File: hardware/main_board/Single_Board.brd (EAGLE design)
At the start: 49.9 x 49.5 mm, 46 parts, among them J1 5520425-3, J2 U.FL, J3 AVR_SPI_PROG_3X2NS, Q1 200mA/40V, Q2 220mA/50V/3.5Ω, Q3 500mA/300V, U1 INA199A3DCKR, U2 MCP1703T-3302E/CB, U3 W25X40CLSNIG, U5 ATMEGA328PB-AU, X1 32.768KHZ-FC-135, X2 B2B-PH-K-S, X3 B2B-XH-2

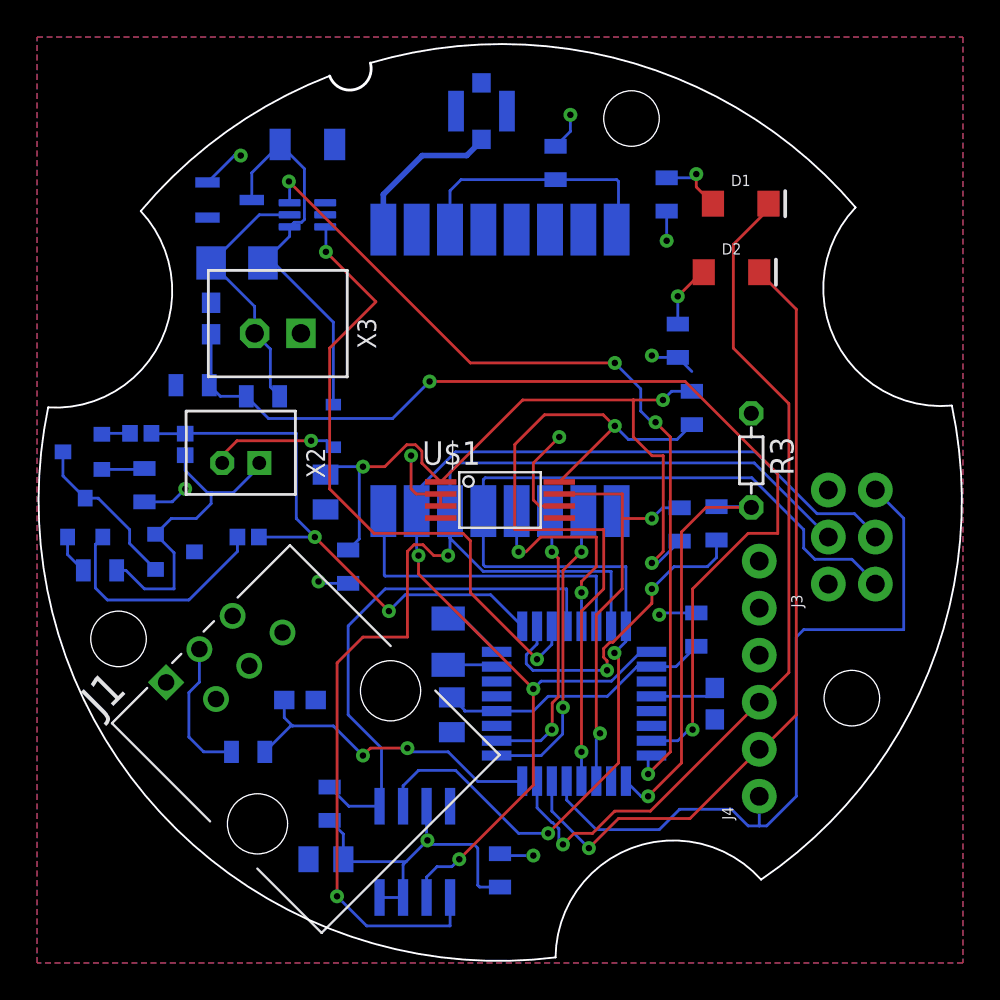
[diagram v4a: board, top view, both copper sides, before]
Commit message: Station improvements. Multi-subpacket handling in receiver. Out of order packets in site datamanager.
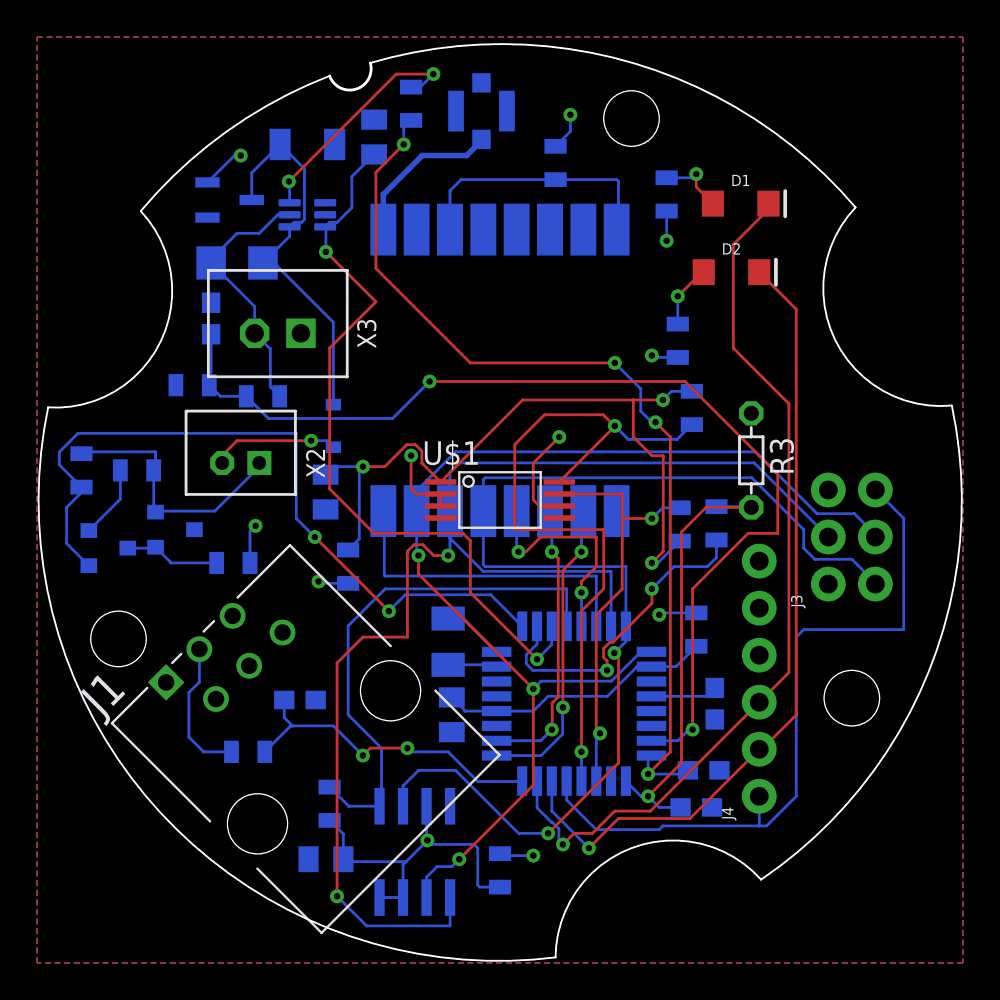
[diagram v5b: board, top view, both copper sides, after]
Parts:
- removed Q3: 500mA/300V, SparkFun-DiscreteSemi:SOT23-3
- removed R19, R20: 500k, SparkFun-Resistors:0402
- added C4, C8: 10nF, SparkFun-Capacitors:0603
- added C9: 1uF, capsmd:0805
- added R15: 10k, SparkFun-Resistors:0805
- Q1: value 200mA/40V -> 220mA/50V/3.5Ω
- R13: value 0 -> 200
- R14: value 20k -> 6k; device SparkFun-Resistors:0402 -> SparkFun-Resistors:0805
- R18: value 0 -> 42k
- R7, R8: value 68k -> 220k
- moved R18 25.1 mm to (20.2, 46.4), turned to 90 degrees
- moved R14 5.77 mm to (2.40, 26.6)
- moved R13 5.76 mm to (5.40, 26.6)
- moved Q1 5.36 mm to (3.80, 22.4), turned to 90 degrees
- moved Q2 1.20 mm to (7.40, 23.4)
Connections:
- removed net N$12: Q1.3, Q2.1, Q3.3
- removed net N$13: Q1.1, R19.1
- net CUR_SENSE: now also C8.2, R18.1; no longer U1.6
- net CUR_SENSE_PWR: now also C9.2
- net GND: now also C4.1, C8.1, C9.1
- net N$10: now also Q1.3, Q2.1, R15.1; no longer Q3.1, R20.1
- net N$3: now also R13.1; no longer R18.1
- net N$5: now also R18.2, U1.6; no longer Q3.2, R13.1
- net N$9: now also R14.2; no longer R14.1
- net PWM_SOLAR: now also Q1.1, R14.1; no longer R14.2, R19.2, R20.2
- net TEMP_SENSE: now also C4.2
- net VCC: now also R15.2; no longer R18.2
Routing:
- net N$5: track 2.15 -> 13.3 mm, vias 0 -> 2
- net PWM_SOLAR: track 30.8 -> 40.6 mm
- net N$12: track 8.83 -> 0.00 mm
- net N$10: track 12.7 -> 5.20 mm
- net CUR_SENSE_PWR: track 35.1 -> 40.3 mm
- net CUR_SENSE: track 48.0 -> 51.2 mm
- net N$9: track 17.3 -> 14.2 mm
- net TEMP_SENSE: track 22.8 -> 24.8 mm
- net N$3: track 2.32 -> 3.95 mm
- net N$13: track 1.54 -> 0.00 mm
- net VCC: track 17.0 -> 15.5 mm
- net AT_RST: track 39.9 -> 39.2 mm

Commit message: Added config for new board Updated Solar PWM for current sensor and impedance switching Fixed a bug with internal termperature sense Added more charge info to detailed weather messages Added support for AVRISP programmer Finalized new board
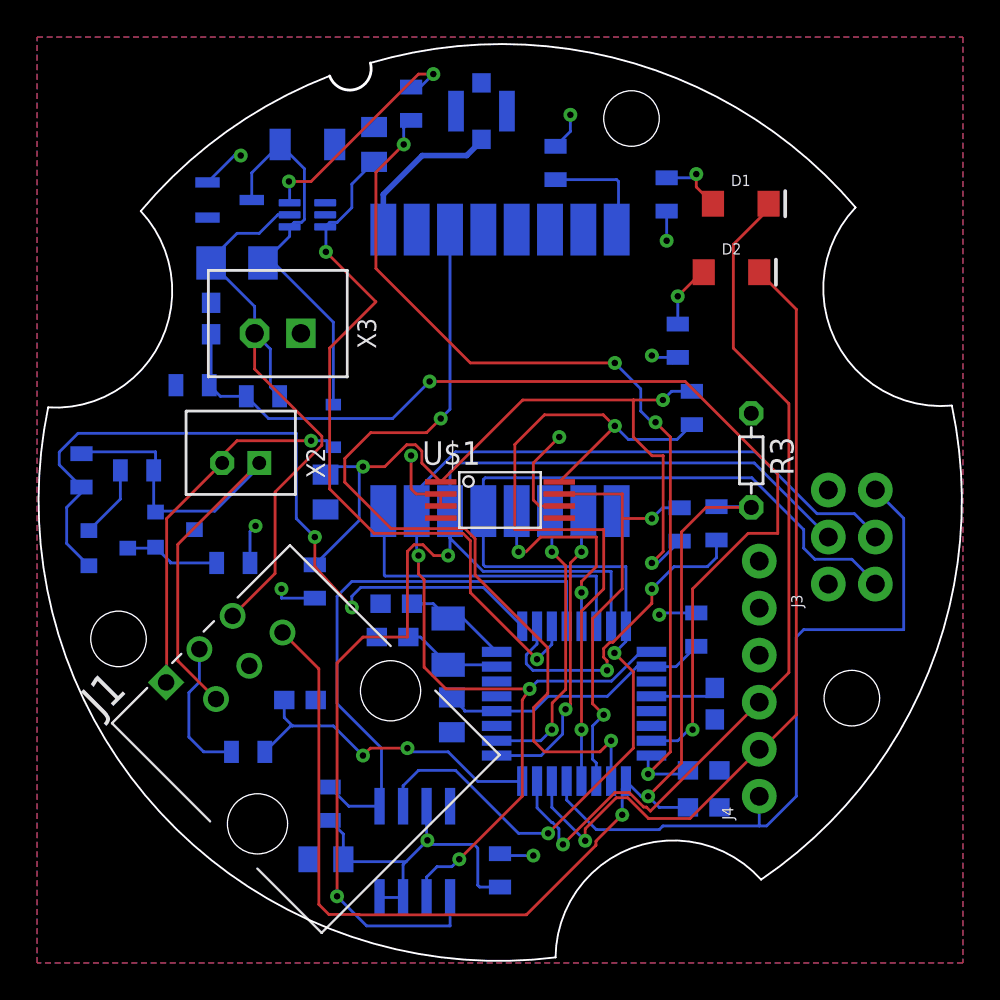
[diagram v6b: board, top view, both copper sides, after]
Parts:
- added C10: 6pF, SparkFun-Capacitors:0603
- added C12: 12pF, SparkFun-Capacitors:0603
- D3: value 0.5A/40V/420mV -> NSR0240HT1G
- Q1: value 220mA/50V/3.5Ω -> 2N7002
- Q2: value 220mA/50V/3.5Ω -> AO3400A
- R13: value 200 -> 20
- R14: value 6k -> 5.6k
- R15: value 10k -> 3.3k
- R18: value 42k -> 47k
- moved R17 1.97 mm to (15.0, 20.6)
- moved C4 0.40 mm to (36.0, 8.40)
- moved C9 0.40 mm to (18.2, 44.2)
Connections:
- removed net N$11: R21.1, R7.1, U1.5, X3.2
- removed net N$9: Q2.2, R13.2, R14.2, X2.1
- new net BATT_+VE: J1.5, R21.1, R7.1, U1.5, X3.2
- new net SOLAR_NEG: J1.2, Q2.2, R13.2, R14.2, X2.1
- new net SX_SW: U$2.SW, U5.26
- net GND: now also C10.1, C12.1
- net N$1: no longer U$2.SW
- net N$7: now also C10.2
- net N$8: now also C12.2
- net TEMP_SENSE: now also J1.6
- net VSOLAR: now also J1.1
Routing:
- net SX_SW: track 0.00 -> 45.8 mm, vias 0 -> 2
- net TEMP_SENSE: track 24.8 -> 61.5 mm, vias 1 -> 2
- net BATT_+VE: track 0.00 -> 32.9 mm
- net SOLAR_NEG: track 0.00 -> 29.6 mm
- net N$11: track 14.2 -> 0.00 mm
- net N$9: track 14.2 -> 0.00 mm
- net VSOLAR: track 6.88 -> 20.0 mm
- net N$1: track 14.1 -> 6.08 mm
- net N$7: track 2.66 -> 5.43 mm
- net SCK: track 62.3 -> 64.9 mm
- net FLASH_SS: track 28.3 -> 30.7 mm
- net N$8: track 3.37 -> 5.65 mm
- net MAG_VCC: track 40.5 -> 42.0 mm
- net PWM_SOLAR: track 40.6 -> 42.1 mm
- net RX: track 43.5 -> 44.3 mm
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
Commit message: Board improvements: Current sensor less prone to latchup Reset pull up resistor JST SH battery connector 8p8c connector to remove shared grounds NPN transistor so we don't operate the mcu outside of spec
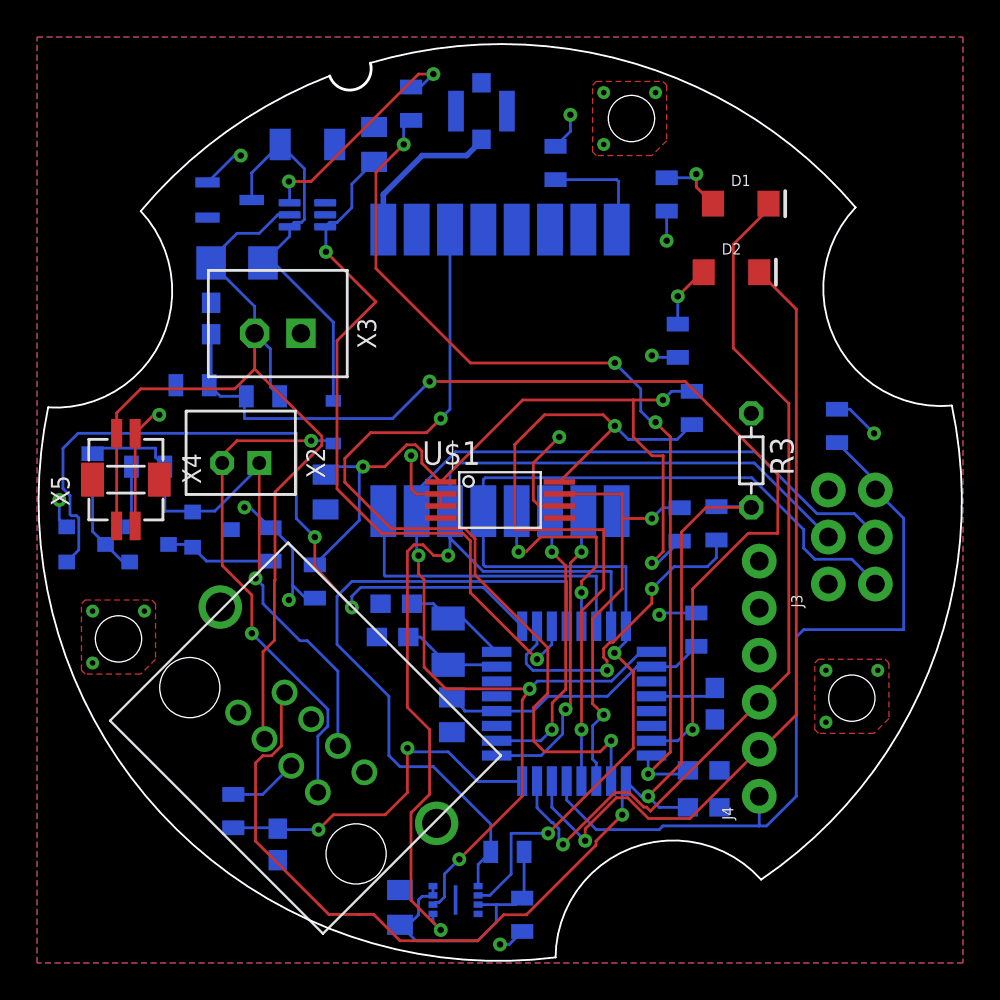
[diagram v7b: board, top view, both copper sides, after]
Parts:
- removed J1: 5520425-3, main_board:TE_5520425-3
- removed U3: W25X40CLSNIG, my-components:WIN_SN-8
- added Q3: S9015, SparkFun-DiscreteSemi:SOT23-3
- added R19: 10k, SparkFun-Resistors:0805
- added U$3: (no value), main_board:RJHSE-3380
- added U4: W25X40CLUXIG_TR, main_board:PSON50P300X200X60-9N
- added X4, X5: BM02B-SRSS-TB, main_board:BM02B-SRSS-TB
- U1: value INA199A3DCKR -> INA199B3DCKR
- U2: value MCP1703T-3302E/CB -> ME6206A25M3G
- moved R9 9.95 mm to (25.4, 6.00), turned to 0 degrees
- moved C2 7.89 mm to (13.0, 6.40), turned to 90 degrees
- moved C7 4.77 mm to (19.6, 3.00), turned to 270 degrees
- moved R6 3.30 mm to (10.6, 8.20), turned to 270 degrees
- moved R16 2.68 mm to (26.2, 2.60), turned to 270 degrees
- moved R15 2.24 mm to (12.6, 22.6), turned to 90 degrees
- moved Q1 2.21 mm to (6.00, 22.6)
- moved Q2 2.00 mm to (9.40, 23.4)
- moved R13 0.63 mm to (6.00, 26.8)
- moved R14 0.60 mm to (3.00, 26.6)
- moved D3 0.20 mm to (16.0, 29.2)
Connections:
- new net EXP: U4.9
- new net N$11: Q1.1, Q3.3, R14.1
- net AT_RST: now also R19.2
- net BATT_+VE: now also U$3.6, X4.2, X5.1; no longer J1.5
- net FLASH_SS: now also U4.1; no longer U3.1
- net FLASH_VCC: now also U4.3, U4.7, U4.8; no longer U3.3, U3.7, U3.8
- net GND: now also U$3.1, U$3.5, U$3.8, U$3.SHLD1, U$3.SHLD2, U4.4, X4.1, X5.2; no longer J1.4, U3.4
- net MISO: now also U4.2; no longer U3.2
- net MOSI: now also U4.5; no longer U3.5
- net N$16: now also U$3.4; no longer J1.3
- net PWM_SOLAR: now also Q3.1; no longer Q1.1, R14.1
- net SCK: now also U4.6; no longer U3.6
- net SOLAR_NEG: now also U$3.3; no longer J1.2
- net TEMP_SENSE: now also U$3.7; no longer J1.6
- net VCC: now also Q3.2, R19.1
- net VSOLAR: now also U$3.2; no longer J1.1
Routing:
- net BATT_+VE: track 32.9 -> 53.5 mm
- net VCC: track 16.2 -> 23.5 mm, vias 8 -> 10
- net VSOLAR: track 20.0 -> 27.2 mm, vias 1 -> 2
- net MOSI: track 73.2 -> 66.4 mm
- net GND: track 9.68 -> 16.4 mm, vias 2 -> 12
- net N$11: track 0.00 -> 5.08 mm
- net FLASH_SS: track 30.7 -> 35.6 mm
- net MISO: track 64.2 -> 60.0 mm
- net N$16: track 7.61 -> 3.77 mm
- net AT_RST: track 39.2 -> 42.6 mm
- net FLASH_VCC: track 18.7 -> 15.4 mm, vias 1 -> 0
- net WIND_SPD: track 17.6 -> 19.6 mm
- net SOLAR_NEG: track 29.6 -> 30.9 mm, vias 0 -> 1
- net PWM_SOLAR: track 42.1 -> 41.3 mm
- net BATT_SENSE: track 56.3 -> 57.1 mm
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- added copper zone on layer 1, net GND

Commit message: Board work for sending off
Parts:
- added R20: 10k, SparkFun-Resistors:0805
- R21: value 0.1 -> 0.5
- U1: value INA199B3DCKR -> INA199B1DCKR
- U2: value ME6206A25M3G -> MCP1703T-3302E/CB
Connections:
- new net N$9: Q3.1, R20.1
- net PWM_SOLAR: now also R20.2; no longer Q3.1
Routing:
- net PWM_SOLAR: track 41.3 -> 26.0 mm
- net N$9: track 0.00 -> 14.1 mm
- net GND: track 16.4 -> 20.7 mm, vias 12 -> 13
- net VCC: track 23.5 -> 27.8 mm
